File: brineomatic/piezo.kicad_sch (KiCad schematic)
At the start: 5 parts, among them Q2 AO3400A

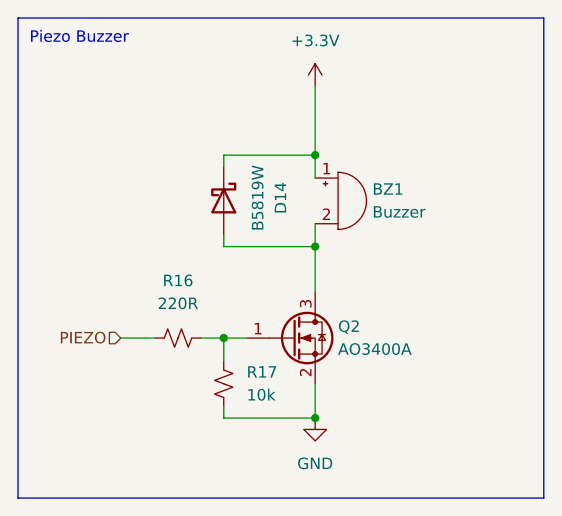
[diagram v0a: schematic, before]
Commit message: added more esd protection to the power rails (24v, 5v, 3.3v)
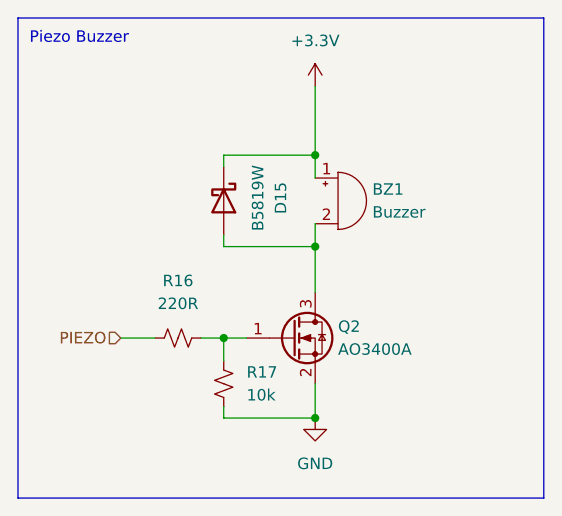
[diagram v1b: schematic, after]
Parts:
- D15: renamed from D14; LCSC (none) -> C7420330
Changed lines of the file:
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@@
 		(on_board yes)
 		(dnp no)
-		(property "Reference" "D14"
+		(property "Reference" "D15"
 			(at 139.7 78.4225 0)
 			(effects
@@
 			)
 		)
-		(property "LCSC" ""
+		(property "LCSC" "C7420330"
 			(at 133.35 78.74 0)
 			(effects
@@
 			(project "brineomatic"
 				(path "/96477ae2-ef08-48f3-8dd4-fe4478541f68/d9651726-ebc8-4cdb-a521-a43a3039a77a"
-					(reference "D14")
+					(reference "D15")
 					(unit 1)
 				)

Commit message: removed old schematics
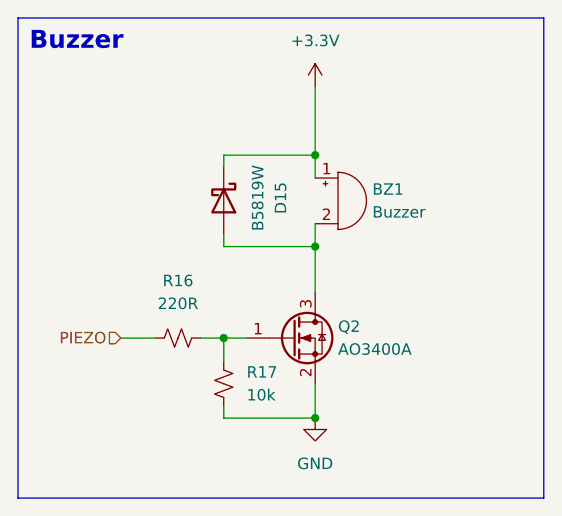
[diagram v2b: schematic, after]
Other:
- note added: "Buzzer"
- note removed: "Piezo Buzzer"
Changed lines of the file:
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@@
 		)
 	)
-	(text "Piezo Buzzer"
+	(text "Buzzer"
 		(exclude_from_sim no)
-		(at 111.76 61.468 0)
+		(at 111.76 62.23 0)
 		(effects
 			(font
-				(size 1.27 1.27)
+				(size 2 2)
+				(thickness 0.4)
+				(bold yes)
 			)
 			(justify left bottom)

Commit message: added a few missing datasheets, switched to new mosfet for buzzer to consolidate bom
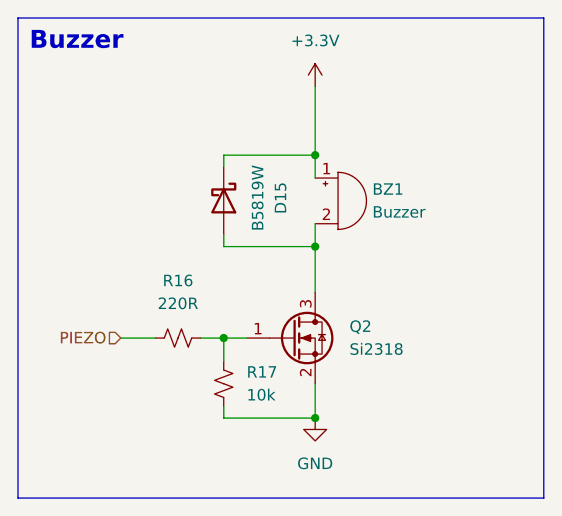
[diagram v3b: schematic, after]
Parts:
- Q2: value AO3400A -> Si2318; LCSC C5224194 -> C14498
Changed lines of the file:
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@@
 		(on_board yes)
 		(dnp no)
+		(fields_autoplaced yes)
 		(property "Reference" "Q2"
-			(at 146.05 92.71 0)
-			(effects
-				(font
-					(size 1.27 1.27)
-				)
-				(justify left)
-			)
-		)
-		(property "Value" "AO3400A"
-			(at 146.05 95.25 0)
+			(at 147.32 92.7099 0)
+			(effects
+				(font
+					(size 1.27 1.27)
+				)
+				(justify left)
+			)
+		)
+		(property "Value" "Si2318"
+			(at 147.32 95.2499 0)
 			(effects
 				(font
@@
 			)
 		)
-		(property "Datasheet" "http://www.aosmd.com/pdfs/datasheet/AO3400A.pdf"
+		(property "Datasheet" "https://www.lcsc.com/datasheet/C14498.pdf"
 			(at 146.05 97.79 0)
 			(effects
@@
 			)
 		)
-		(property "Description" "30V Vds, 5.7A Id, N-Channel MOSFET, SOT-23"
+		(property "Description" "MOSFET N-CH 40V 5.6A SOT-23"
 			(at 140.97 93.98 0)
 			(effects
@@
 			)
 		)
-		(property "LCSC" "C5224194"
+		(property "LCSC" "C14498"
 			(at 140.97 93.98 0)
 			(effects
@@
 			)
 		)
-		(property "ALT" ""
-			(at 140.97 93.98 0)
-			(effects
-				(font
-					(size 1.27 1.27)
-				)
-				(hide yes)
-			)
-		)
-		(property "LCSC Part Name" ""
-			(at 140.97 93.98 0)
-			(effects
-				(font
-					(size 1.27 1.27)
-				)
-				(hide yes)
-			)
-		)
-		(property "Manufacturer" ""
-			(at 140.97 93.98 0)
-			(effects
-				(font
-					(size 1.27 1.27)
-				)
-				(hide yes)
-			)
-		)
-		(property "Manufacturer Part" ""
-			(at 140.97 93.98 0)
-			(effects
-				(font
-					(size 1.27 1.27)
-				)
-				(hide yes)
-			)
-		)
-		(property "Supplier" ""
-			(at 140.97 93.98 0)
-			(effects
-				(font
-					(size 1.27 1.27)
-				)
-				(hide yes)
-			)
-		)
-		(property "Supplier Part" ""
-			(at 140.97 93.98 0)
-			(effects
-				(font
-					(size 1.27 1.27)
-				)
-				(hide yes)
-			)
+		(pin "2"
+		)
+		(pin "3"
 		)
 		(pin "1"
-		)
-		(pin "2"
-		)
-		(pin "3"
 		)
 		(instances
@@
 				(path "/96477ae2-ef08-48f3-8dd4-fe4478541f68/d9651726-ebc8-4cdb-a521-a43a3039a77a"
 					(reference "Q2")
-					(unit 1)
-				)
-			)
-			(project "sendit"
-				(path "/a355e4d0-2918-44fc-be8d-2503b84c6d6c/730ddc54-308b-4950-8f3a-2beb2098c60b"
-					(reference "Q1")
 					(unit 1)
 				)
@@
 			)
 		)
-		(property "Datasheet" "~"
+		(property "Datasheet" "https://www.lcsc.com/datasheet/C96256.pdf"
 			(at 145.415 76.2 90)
 			(effects

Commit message: tested and update bom + placement
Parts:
- D15: Rotation Offset (none) -> 180
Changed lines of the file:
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@@
+			)
+		)
+		(property "Rotation Offset" "180"
+			(at 133.35 78.74 0)
+			(effects
+				(font
+					(size 1.27 1.27)
+				)
+				(hide yes)
 			)
 		)

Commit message: updated resistor p/ns in bom
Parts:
- R16: LCSC (none) -> C22962
- R17: LCSC (none) -> C25804
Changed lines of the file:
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@@
+			)
+		)
+		(property "LCSC" " C22962"
+			(at 128.27 93.98 90)
+			(effects
+				(font
+					(size 1.27 1.27)
+				)
+				(hide yes)
 			)
 		)
@@
 			(at 133.35 99.06 0)
 			(effects
+				(font
+					(size 1.27 1.27)
+				)
+				(hide yes)
+			)
+		)
+		(property "LCSC" "C25804"
+			(at 133.35 99.06 0)
+			(effects

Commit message: added esd protection to relay driver connector
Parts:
- renumbered D15 to D16
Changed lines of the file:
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@@
 		(on_board yes)
 		(dnp no)
-		(property "Reference" "D15"
+		(property "Reference" "D16"
 			(at 139.7 78.4225 0)
 			(effects
@@
 			(project "brineomatic"
 				(path "/96477ae2-ef08-48f3-8dd4-fe4478541f68/d9651726-ebc8-4cdb-a521-a43a3039a77a"
-					(reference "D15")
+					(reference "D16")
 					(unit 1)
 				)

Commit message: add inline resistor to temperature sensor + servo inputs - 100ohm
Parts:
- renumbered R16 to R19, R17 to R20
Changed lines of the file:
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@@
 		(dnp no)
 		(fields_autoplaced yes)
-		(property "Reference" "R16"
+		(property "Reference" "R19"
 			(at 128.27 87.63 90)
 			(effects
@@
 			(project "brineomatic"
 				(path "/96477ae2-ef08-48f3-8dd4-fe4478541f68/d9651726-ebc8-4cdb-a521-a43a3039a77a"
-					(reference "R16")
+					(reference "R19")
 					(unit 1)
 				)
@@
 		(dnp no)
 		(fields_autoplaced yes)
-		(property "Reference" "R17"
+		(property "Reference" "R20"
 			(at 135.89 97.7899 0)
 			(effects
@@
 			(project "brineomatic"
 				(path "/96477ae2-ef08-48f3-8dd4-fe4478541f68/d9651726-ebc8-4cdb-a521-a43a3039a77a"
-					(reference "R17")
-					(unit 1)
-				)
+					(reference "R20")
+					(unit 1)
+				)

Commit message: updated analog sensor esd schematic
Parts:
- renumbered D16 to D17
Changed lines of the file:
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@@
 		(on_board yes)
 		(dnp no)
-		(property "Reference" "#PWR024"
+		(property "Reference" "#PWR025"
 			(at 143.51 69.85 0)
 			(effects
@@
 			(project "brineomatic"
 				(path "/96477ae2-ef08-48f3-8dd4-fe4478541f68/d9651726-ebc8-4cdb-a521-a43a3039a77a"
-					(reference "#PWR024")
+					(reference "#PWR025")
 					(unit 1)
 				)
@@
 		(on_board yes)
 		(dnp no)
-		(property "Reference" "D16"
+		(property "Reference" "D17"
 			(at 139.7 78.4225 0)
 			(effects
@@
 			(project "brineomatic"
 				(path "/96477ae2-ef08-48f3-8dd4-fe4478541f68/d9651726-ebc8-4cdb-a521-a43a3039a77a"
-					(reference "D16")
+					(reference "D17")
 					(unit 1)
 				)
@@
 		(dnp no)
 		(fields_autoplaced yes)
-		(property "Reference" "#PWR025"
+		(property "Reference" "#PWR026"
 			(at 143.51 109.22 0)
 			(effects
@@
 			(project "brineomatic"
 				(path "/96477ae2-ef08-48f3-8dd4-fe4478541f68/d9651726-ebc8-4cdb-a521-a43a3039a77a"
-					(reference "#PWR025")
-					(unit 1)
-				)
+					(reference "#PWR026")
+					(unit 1)
+				)
